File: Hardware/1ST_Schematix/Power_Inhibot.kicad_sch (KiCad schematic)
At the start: 41 parts, among them J301 USB_C_Receptacle_USB2.0_16P, Q301 MMDT2222A, Q302 DMP1045U-7, Q303 DMN313DLT-7, U301 USBLC6-2SC6, U302 BQ25896RTW, U303 BQ27220YZFR, U304 LP2985-3.3

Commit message: first
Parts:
- removed Q303: DMN313DLT-7, Package_TO_SOT_SMD:SOT-523, symbol Transistor_FET:DMN3150L
- removed R314: 10m, symbol Device:R
- removed R315: 10k, symbol Device:R
- removed R316: 100, symbol Device:R
- added D301: D, Diode_THT:Diode_Bridge_IXYS_GUFP, symbol Device:D
- C302: value 470n -> C
- C303: value 2.2u -> C
- R306: value 10k -> 1k
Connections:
- net Jauge_SCL is gone; now on net BMS_SCL: U303.A2 (SDA)
- net Jauge_SDA is gone; now on net BMS_SDA: U303.A3 (SCL)
- net +5V: no longer R306.2
- net GND: now also R306.2
- net USB_5V: now also D301.1 (K)
- net VBAT: no longer C311.1, U303.C1 (SRP), U303.C3 (BAT)
- net at Q301.2 (B1), Q301.3 (C2), Q301.5 (B2)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: now also D301.2 (A)
- new net: C311.1, U303.C3 (BAT)
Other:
- moved on the sheet: Q301A, Q301B, Q302, R301, R304

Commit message: Update before INT
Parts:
- removed D301: D, Diode_THT:Diode_Bridge_IXYS_GUFP, symbol Device:D
- added Q303: DMN313DLT-7, Package_TO_SOT_SMD:SOT-523, symbol Transistor_FET:DMN3110S
- added R314: 100, Package_TO_SOT_SMD:SOT-363_SC-70-6, symbol Device:R_Small
- added R315, R316: 10k, Package_TO_SOT_SMD:SOT-363_SC-70-6, symbol Device:R_Small
- R306: value 1k -> 10m
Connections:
- net VBUS is gone; now on net +5V: Q301.6 (C1), Q302.2 (S), U302.1 (VBUS)
- net +5V: now also R316.1
- net GND: now also Q303.2 (S), R315.2; no longer R306.2
- net USB_5V: now also R314.1
- net VBAT: now also R306.2, U303.C1 (SRP)
- net at U302.8 (OTG): now also Q303.3 (D), R316.2; no longer R306.1
- net at U303.C2 (SRN): now also R306.1
- new net: Q303.1 (G), R314.2, R315.1
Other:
- moved on the sheet: C302, C303, Q301A, Q301B, Q302, R301, R304

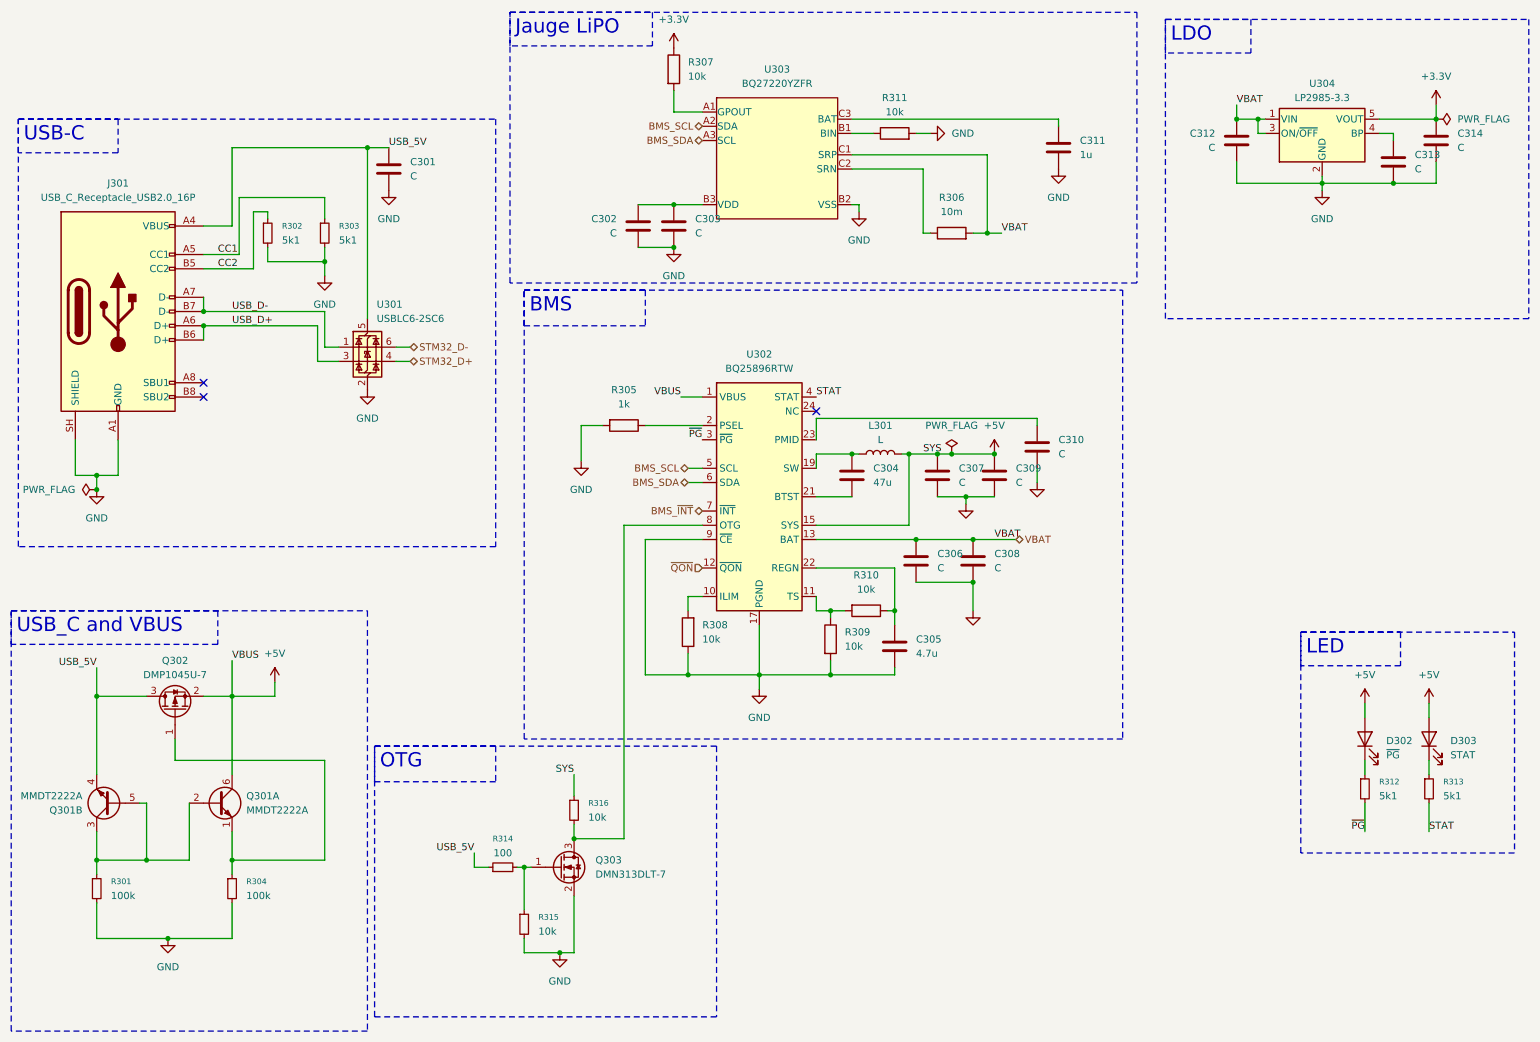
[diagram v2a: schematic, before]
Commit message: Update KiCad and STM32CubeMX
Ready for the check-in
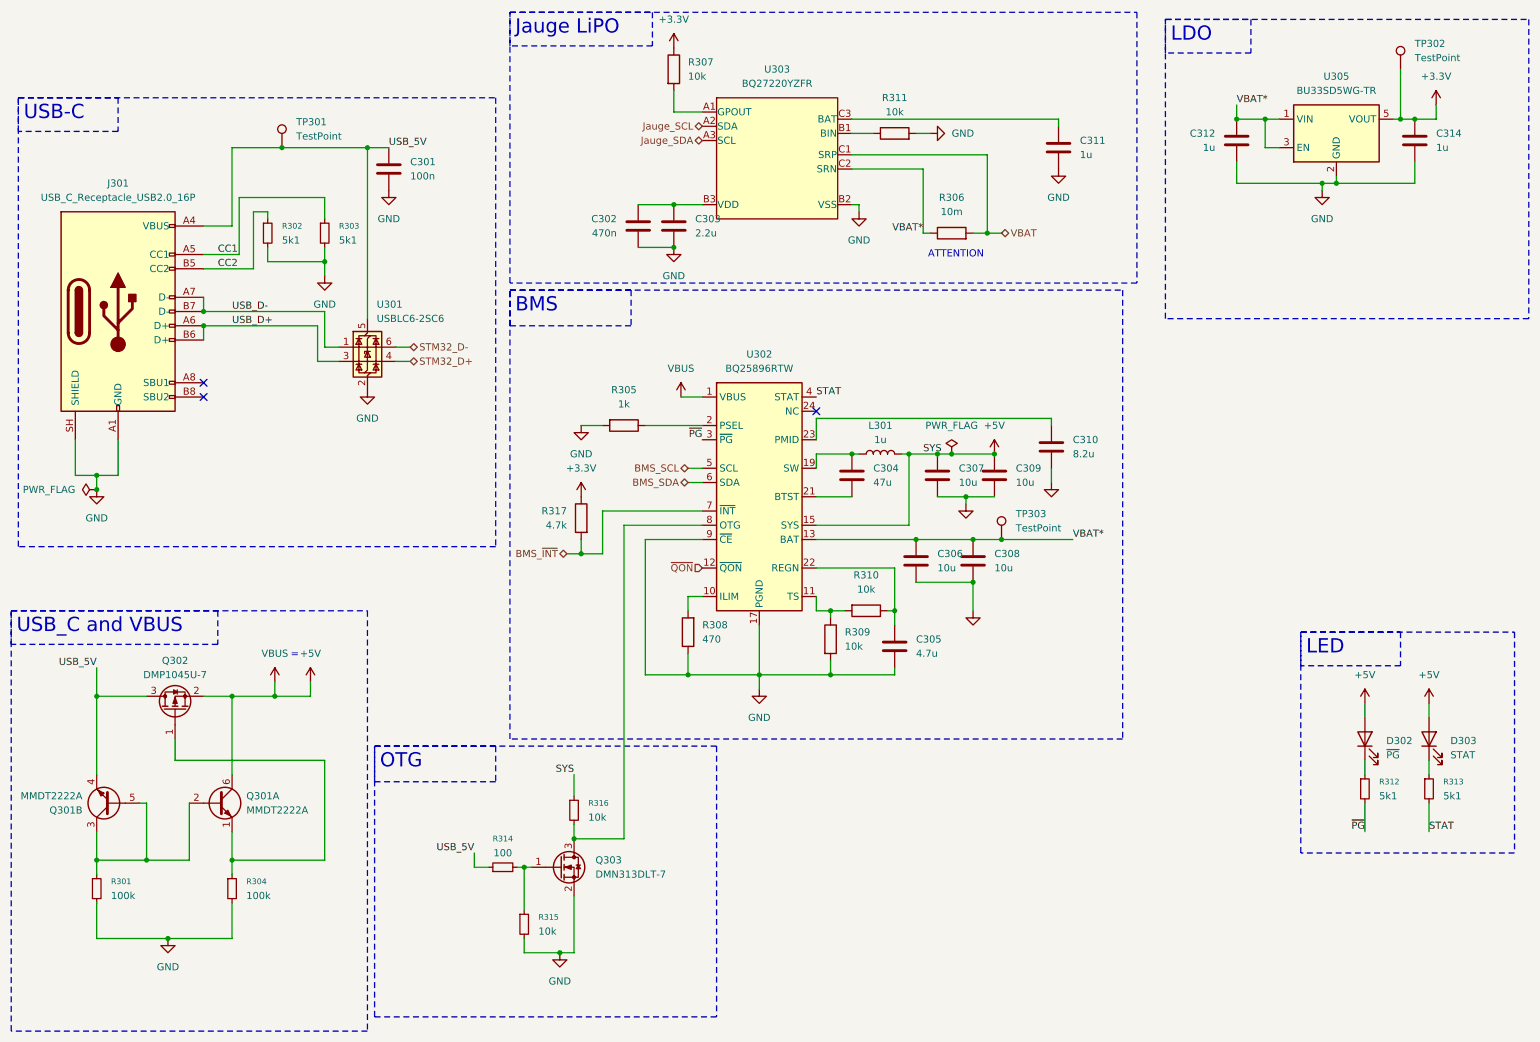
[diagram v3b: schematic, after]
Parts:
- removed C313: C, Capacitor_SMD:C_0402_1005Metric, symbol Device:C
- removed U304: LP2985-3.3, Package_TO_SOT_SMD:SOT-23-5, symbol Regulator_Linear:LP2985-3.3
- added R317: 4.7k, symbol Device:R
- added TP301, TP302, TP303: TestPoint, TestPoint:TestPoint_Pad_D2.0mm, symbol Connector:TestPoint
- added U305: BU33SD5WG-TR, Package_TO_SOT_SMD:TSOT-23-5, symbol Regulator_Linear:MIC5365-3.3YD5
- C301: value C -> 100n
- C302: value C -> 470n
- C303: value C -> 2.2u
- C306, C307, C308, C309: value C -> 10u
- C310: value C -> 8.2u
- C312, C314: value C -> 1u
- L301: value L -> 1u
- R308: value 10k -> 470
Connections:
- net +3.3V: now also R317.1, TP302.1, U305.5 (VOUT)
- net BMS_SCL: no longer U303.A2 (SDA)
- net BMS_SDA: no longer U303.A3 (SCL)
- net BMS_~{INT}: now also R317.2
- net GND: now also U305.2 (GND)
- net USB_5V: now also TP301.1
- net VBAT: no longer C306.1, C308.1, C312.1, U302.13 (BAT), U302.14 (BAT)
- net VBAT*: now reaches R306.1, U303.C2 (SRN)
- net VBAT*: now also C306.1, C308.1, C312.1, U302.13 (BAT), U302.14 (BAT), TP303.1, U305.1 (VIN), U305.3 (EN)
- new net Jauge_SCL: U303.A2 (SDA)
- new net Jauge_SDA: U303.A3 (SCL)
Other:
- note added: "="
- note added: "ATTENTION"
- moved on the sheet: C310, C314

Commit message: Update Schematic
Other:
- note removed: "="
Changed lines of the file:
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@@
 		)
 	)
-	(text "="
-		(exclude_from_sim no)
-		(at 61.976 127.254 0)
-		(effects
-			(font
-				(size 1.27 1.27)
-			)
-		)
-	)
 	(text "ATTENTION"
 		(exclude_from_sim no)
@@
 	)
 	(junction
-		(at 58.42 134.62)
-		(diameter 0)
-		(color 0 0 0 0)
-	)
-	(junction
 		(at 157.48 119.38)
 		(diameter 0)
@@
 	(wire
 		(pts
-			(xy 58.42 134.62) (xy 50.8 134.62)
+			(xy 50.8 134.62) (xy 64.77 134.62)
 		)
 		(stroke
@@
 	(wire
 		(pts
-			(xy 64.77 134.62) (xy 58.42 134.62)
-		)
-		(stroke
-			(width 0)
-			(type default)
-		)
-	)
-	(wire
-		(pts
 			(xy 113.03 106.68) (xy 113.03 109.22)
 		)
@@
 	(wire
 		(pts
-			(xy 58.42 132.08) (xy 58.42 134.62)
-		)
-		(stroke
-			(width 0)
-			(type default)
-		)
-	)
-	(wire
-		(pts
 			(xy 154.94 116.84) (xy 154.94 119.38)
 		)
@@
 	)
 	(symbol
-		(lib_id "power:VBUS")
-		(at 58.42 132.08 0)
-		(unit 1)
-		(body_style 1)
-		(exclude_from_sim no)
-		(in_bom yes)
-		(on_board yes)
-		(in_pos_files yes)
-		(dnp no)
-		(fields_autoplaced yes)
-		(property "Reference" "#PWR0323"
-			(at 58.42 135.89 0)
-			(hide yes)
-			(show_name no)
-			(do_not_autoplace no)
-			(effects
-				(font
-					(size 1.27 1.27)
-				)
-			)
-		)
-		(property "Value" "VBUS"
-			(at 58.42 127 0)
-			(show_name no)
-			(do_not_autoplace no)
-			(effects
-				(font
-					(size 1.27 1.27)
-				)
-			)
-		)
-		(property "Footprint" ""
-			(at 58.42 132.08 0)
-			(hide yes)
-			(show_name no)
-			(do_not_autoplace no)
-			(effects
-				(font
-					(size 1.27 1.27)
-				)
-			)
-		)
-		(property "Datasheet" ""
-			(at 58.42 132.08 0)
-			(hide yes)
-			(show_name no)
-			(do_not_autoplace no)
-			(effects
-				(font
-					(size 1.27 1.27)
-				)
-			)
-		)
-		(property "Description" "Power symbol creates a global label with name \"VBUS\""
-			(at 58.42 132.08 0)
-			(hide yes)
-			(show_name no)
-			(do_not_autoplace no)
-			(effects
-				(font
-					(size 1.27 1.27)
-				)
-			)
-		)
-		(pin "1"
-		)
-		(instances
-			(project "1ST_Schematix"
-				(path "/59c2502d-7c28-4023-9b54-15ec9e15e6d4/58991d82-9dd2-4511-b974-9bfcbd0b4f51"
-					(reference "#PWR0323")
-					(unit 1)
-				)
-			)
-		)
-	)
-	(symbol
 		(lib_id "power:+3.3V")
 		(at 265.43 29.21 0)
@@
 	)
 	(symbol
+		(lib_id "power:+5V")
+		(at 130.81 81.28 0)
+		(unit 1)
+		(body_style 1)
+		(exclude_from_sim no)
+		(in_bom yes)
+		(on_board yes)
+		(in_pos_files yes)
+		(dnp no)
+		(fields_autoplaced yes)
+		(property "Reference" "#PWR0322"
+			(at 130.81 85.09 0)
+			(hide yes)
+			(show_name no)
+			(do_not_autoplace no)
+			(effects
+				(font
+					(size 1.27 1.27)
+				)
+			)
+		)
+		(property "Value" "+5V"
+			(at 130.81 76.2 0)
+			(show_name no)
+			(do_not_autoplace no)
+			(effects
+				(font
+					(size 1.27 1.27)
+				)
+			)
+		)
+		(property "Footprint" ""
+			(at 130.81 81.28 0)
+			(hide yes)
+			(show_name no)
+			(do_not_autoplace no)
+			(effects
+				(font
+					(size 1.27 1.27)
+				)
+			)
+		)
+		(property "Datasheet" ""
+			(at 130.81 81.28 0)
+			(hide yes)
+			(show_name no)
+			(do_not_autoplace no)
+			(effects
+				(font
+					(size 1.27 1.27)
+				)
+			)
+		)
+		(property "Description" "Power symbol creates a global label with name \"+5V\""
+			(at 130.81 81.28 0)
+			(hide yes)
+			(show_name no)
+			(do_not_autoplace no)
+			(effects
+				(font
+					(size 1.27 1.27)
+				)
+			)
+		)
+		(pin "1"
+		)
+		(instances
+			(project "1ST_Schematix"
+				(path "/59c2502d-7c28-4023-9b54-15ec9e15e6d4/58991d82-9dd2-4511-b974-9bfcbd0b4f51"
+					(reference "#PWR0322")
+					(unit 1)
+				)
+			)
+		)
+	)
+	(symbol
 		(lib_id "Regulator_Linear:MIC5365-3.3YD5")
 		(at 247.65 34.29 0)
@@
 					(unit 1)
 				)
-			)
-		)
-	)
-	(symbol
-		(lib_id "power:VBUS")
-		(at 130.81 81.28 0)
-		(unit 1)
-		(body_style 1)
-		(exclude_from_sim no)
-		(in_bom yes)
-		(on_board yes)
-		(in_pos_files yes)
-		(dnp no)
-		(fields_autoplaced yes)
-		(property "Reference" "#PWR0322"
-			(at 130.81 85.09 0)
-			(hide yes)
-			(show_name no)
-			(do_not_autoplace no)
-			(effects
-				(font
-					(size 1.27 1.27)
-				)
-			)
-		)
-		(property "Value" "VBUS"
-			(at 130.81 76.2 0)
-			(show_name no)
-			(do_not_autoplace no)
-			(effects
-				(font
-					(size 1.27 1.27)
-				)
-			)
-		)
-		(property "Footprint" ""
-			(at 130.81 81.28 0)
-			(hide yes)
-			(show_name no)
-			(do_not_autoplace no)
-			(effects
-				(font
-					(size 1.27 1.27)
-				)
-			)
-		)
-		(property "Datasheet" ""
-			(at 130.81 81.28 0)
-			(hide yes)
-			(show_name no)
-			(do_not_autoplace no)
-			(effects
-				(font
-					(size 1.27 1.27)
-				)
-			)
-		)
-		(property "Description" "Power symbol creates a global label with name \"VBUS\""
-			(at 130.81 81.28 0)
-			(hide yes)
-			(show_name no)
-			(do_not_autoplace no)
-			(effects
-				(font
-					(size 1.27 1.27)
-				)
-			)
-		)
-		(pin "1"
-		)
-		(instances
-			(project "1ST_Schematix"
-				(path "/59c2502d-7c28-4023-9b54-15ec9e15e6d4/58991d82-9dd2-4511-b974-9bfcbd0b4f51"
-					(reference "#PWR0322")
-					(unit 1)
-				)

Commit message: schematic review with esteemed professor
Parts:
- added J302: Conn_01x02, symbol Connector_Generic:Conn_01x02
- added JP301, JP302, JP303: SolderJumper_2_Open, Jumper:SolderJumper-2_P1.3mm_Open_TrianglePad1.0x1.5mm, symbol Jumper:SolderJumper_2_Open
- added TP304, TP305: TestPoint, TestPoint:TestPoint_Pad_D2.0mm, symbol Connector:TestPoint
- C301: JLCPCB Part # (none) -> C1525
- C304: value 47u -> 47n
- C305: value 4.7u -> 4u7
- D302, D303: footprint Package_DFN_QFN:Texas_RTW_WQFN-24-1EP_4x4mm_P0.5mm_EP2.7x2.7mm_ThermalVias -> LED_SMD:LED_0603_1608Metric
- R301, R304, R314, R315, R316: footprint Package_TO_SOT_SMD:SOT-363_SC-70-6 -> Resistor_SMD:R_0402_1005Metric
- R305, R307, R309, R310, R311: footprint (none) -> Resistor_SMD:R_0402_1005Metric
- R308: value 470 -> 470R; footprint (none) -> Resistor_SMD:R_0402_1005Metric
- R317: value 4.7k -> 4k7; footprint (none) -> Resistor_SMD:R_0402_1005Metric
- TP301, TP302, TP303: now left out of the parts list
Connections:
- net VBAT is gone; now on net +BATT: R306.2, U303.C1 (SRP)
- net +5V: now also JP303.2 (B); no longer C307.1, C309.1, D302.2 (A), D303.2 (A), L301.2, Q301.6 (C1), Q302.2 (S), R316.1, U302.1 (VBUS), U302.15 (SYS), U302.16 (SYS)
- net GND: now also J302.2 (Pin_2), TP305.1
- net Jauge_SCL: now also U303.A3 (SCL); no longer U303.A2 (SDA)
- net Jauge_SDA: now also U303.A2 (SDA); no longer U303.A3 (SCL)
- net USB_5V: now also JP301.2 (B); no longer C301.1, J301.A4 (VBUS), J301.A9 (VBUS), J301.B4 (VBUS), J301.B9 (VBUS), U301.5 (VBUS)
- net REGN: now reaches C305.2, R310.1, U302.22 (REGN)
- net +BATT: now reaches C311.1, U303.C3 (BAT)
- net +BATT: now also J302.1 (Pin_1)
- net VBAT* renamed VBAT_TO_SHUNT
- net VBAT_TO_SHUNT: no longer C312.1, U305.1 (VIN), U305.3 (EN)
- new net: C307.1, C309.1, JP302.1 (A), L301.2, U302.15 (SYS), U302.16 (SYS)
- new net: C301.1, J301.A4 (VBUS), J301.A9 (VBUS), J301.B4 (VBUS), J301.B9 (VBUS), JP301.1 (A), U301.5 (VBUS)
- new net SYS: C312.1, D302.2 (A), D303.2 (A), JP302.2 (B), R316.1, TP304.1, U305.1 (VIN), U305.3 (EN)
- new net VBUS: JP303.1 (A), Q301.6 (C1), Q302.2 (S), U302.1 (VBUS)
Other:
- moved on the sheet: C310, R306, TP301

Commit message: prints for component except 10mOhm
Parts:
- J302: footprint (none) -> Connector_JST:JST_EH_B2B-EH-A_1x02_P2.50mm_Vertical
- R306: JLCPCB Part # (none) -> C503807
- TP301, TP302, TP303, TP304, TP305: now in the parts list
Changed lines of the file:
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@@
 		(body_style 1)
 		(exclude_from_sim no)
-		(in_bom no)
+		(in_bom yes)
 		(on_board yes)
 		(in_pos_files yes)
@@
 		(body_style 1)
 		(exclude_from_sim no)
-		(in_bom no)
+		(in_bom yes)
 		(on_board yes)
 		(in_pos_files yes)
@@
 			)
 		)
+		(property "JLCPCB Part #" "C503807"
+			(at 184.15 52.07 90)
+			(hide yes)
+			(show_name no)
+			(do_not_autoplace no)
+			(effects
+				(font
+					(size 1.27 1.27)
+				)
+			)
+		)
 		(pin "2"
 		)
@@
 		(body_style 1)
 		(exclude_from_sim no)
-		(in_bom no)
+		(in_bom yes)
 		(on_board yes)
 		(in_pos_files yes)
@@
 		(body_style 1)
 		(exclude_from_sim no)
-		(in_bom no)
+		(in_bom yes)
 		(on_board yes)
 		(in_pos_files yes)
@@
 			)
 		)
-		(property "Footprint" ""
+		(property "Footprint" "Connector_JST:JST_EH_B2B-EH-A_1x02_P2.50mm_Vertical"
 			(at 255.27 85.09 0)
 			(hide yes)
@@
 		(body_style 1)
 		(exclude_from_sim no)
-		(in_bom no)
+		(in_bom yes)
 		(on_board yes)
 		(in_pos_files yes)

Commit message: all footprints done
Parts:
- R306: footprint (none) -> Resistor_SMD:R_2512_6332Metric; JLCPCB Part # C503807 -> C105142
